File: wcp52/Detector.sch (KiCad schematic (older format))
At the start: 13 parts, among them U10 AD8310ARMZ

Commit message: BOM line fixes
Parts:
- C63, C65, C67, C68, C69, C70, C71, R78, R79, R80: Manuf Value -> (none)
- C64, C66: Description (none) -> CAP MLCC 1uF [0805]
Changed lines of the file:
@@
 EESchema Schematic File Version 2
+LIBS:Altera
+LIBS:AnalogDevices
+LIBS:Atmel
+LIBS:conn-2mm
+LIBS:conn-100mil
+LIBS:conn-cui
+LIBS:conn-fci
+LIBS:conn-linx
+LIBS:conn-molex
+LIBS:conn-tagconnect
+LIBS:conn-test
+LIBS:DiodesInc
+LIBS:display
+LIBS:_electromech
+LIBS:Fairchild
+LIBS:FTDI
+LIBS:Intersil
+LIBS:Lattice
+LIBS:_linear
+LIBS:LinearTech
+LIBS:Littelfuse
+LIBS:logic-4000
+LIBS:logic-7400
+LIBS:MACOM
+LIBS:maxim
+LIBS:mechanical
+LIBS:Microchip
+LIBS:Micron
+LIBS:NXP
+LIBS:onsemi
+LIBS:passive
+LIBS:pasv-BiTech
+LIBS:pasv-Bourns
+LIBS:pasv-cap
+LIBS:pasv-ind
+LIBS:pasv-res
+LIBS:pcb
+LIBS:power
+LIBS:_semi
+LIBS:semi-diode-1N
+LIBS:semi-diode-BA
+LIBS:semi-diode-MCC
+LIBS:semi-diode-MMB
+LIBS:semi-diode-NXP
+LIBS:semi-diode-OnSemi
+LIBS:semi-diode-Vishay
+LIBS:semi-opto-misc
+LIBS:semi-thyristor-2N
+LIBS:semi-trans-2N
+LIBS:semi-trans-AO
+LIBS:semi-trans-BC
+LIBS:semi-trans-DiodesInc
+LIBS:semi-trans-Fairchild
+LIBS:semi-trans-Infineon
+LIBS:semi-trans-IntRect
+LIBS:semi-trans-IXYS
+LIBS:semi-trans-misc
+LIBS:semi-trans-MMB
+LIBS:semi-trans-MPS
+LIBS:semi-trans-NXP
+LIBS:semi-trans-PZT
+LIBS:semi-trans-TI
+LIBS:semi-trans-TIP
+LIBS:semi-trans-Toshiba
+LIBS:silabs
+LIBS:skyworks
+LIBS:ST
+LIBS:st_ic
+LIBS:st_semi
+LIBS:supertex
+LIBS:symbol
+LIBS:TexasInstruments
+LIBS:vishay_semi
+LIBS:Xilinx
+LIBS:pasv-xtal
+LIBS:conn-te
 LIBS:wcp52-cache
 EELAYER 25 0
@@
 F 5 "TDK" H 3700 3600 60  0001 C CNN "Manuf"
 F 6 "DIST DIGIKEY 445-11490-1-ND" H 4500 4150 60  0001 C CNN "BOM"
-F 7 "C78" H 3700 3600 50  0001 C CNN "OldReference"
+F 7 "CAP MLCC 1uF [0805]" H 3700 3600 60  0001 C CNN "Description"
+F 8 "C78" H 3700 3600 50  0001 C CNN "OldReference"
 	1    3700 3600
 	0    1    1    0
@@
 F 5 "TDK" H 3700 4400 60  0001 C CNN "Manuf"
 F 6 "DIST DIGIKEY 445-11490-1-ND" H 4500 4950 60  0001 C CNN "BOM"
-F 7 "C80" H 3700 4400 50  0001 C CNN "OldReference"
+F 7 "CAP MLCC 1uF [0805]" H 3700 4400 60  0001 C CNN "Description"
+F 8 "C80" H 3700 4400 50  0001 C CNN "OldReference"
 	1    3700 4400
 	0    1    1    0
@@
 F 2 "IPC7351-Nominal:CAPC1608X55" H 8200 3800 50  0001 C CNN
 F 3 "" H 8190 3775 60  0000 C CNN
-F 4 "Value" H 8200 3800 60  0001 C CNN "Manuf"
+F 4 "" H 8200 3800 60  0001 C CNN "Manuf"
 F 5 "CAP MLCC 220p C0G 16V 5% [0603]" H 9000 4350 60  0001 C CNN "BOM"
 F 6 "C84" H 8200 3800 50  0001 C CNN "OldReference"
@@
 F 2 "IPC7351-Nominal:CAPC1608X55" H 8200 4600 50  0001 C CNN
 F 3 "" H 8190 4575 60  0000 C CNN
-F 4 "Value" H 8200 4600 60  0001 C CNN "Manuf"
+F 4 "" H 8200 4600 60  0001 C CNN "Manuf"
 F 5 "CAP MLCC 330n ≥X7R 50V 5% [0603]" H 9000 5150 60  0001 C CNN "BOM"
 F 6 "C85" H 8200 4600 50  0001 C CNN "OldReference"
@@
 F 2 "IPC7351-Nominal:CAPC3216X70" H 7100 2700 50  0001 C CNN
 F 3 "" H 7090 2675 60  0000 C CNN
-F 4 "Value" H 7100 2700 60  0001 C CNN "Manuf"
+F 4 "" H 7100 2700 60  0001 C CNN "Manuf"
 F 5 "CAP MLCC 47u ≥X5R 10V 20% [1206]" H 7900 3250 60  0001 C CNN "BOM"
 F 6 "C83" H 7100 2700 50  0001 C CNN "OldReference"
@@
 F 2 "IPC7351-Nominal:CAPC1608X55" H 3700 3400 50  0001 C CNN
 F 3 "" H 3690 3375 60  0000 C CNN
-F 4 "Value" H 3700 3400 60  0001 C CNN "Manuf"
+F 4 "" H 3700 3400 60  0001 C CNN "Manuf"
 F 5 "CAP MLCC 10n ≥X5R 50V 10% [0603]" H 4500 3950 60  0001 C CNN "BOM"
 F 6 "C57" H 3700 3400 50  0001 C CNN "OldReference"
@@
 F 2 "IPC7351-Nominal:CAPC1608X55" H 3700 4200 50  0001 C CNN
 F 3 "" H 3690 4175 60  0000 C CNN
-F 4 "Value" H 3700 4200 60  0001 C CNN "Manuf"
+F 4 "" H 3700 4200 60  0001 C CNN "Manuf"
 F 5 "CAP MLCC 10n ≥X5R 50V 10% [0603]" H 4500 4750 60  0001 C CNN "BOM"
 F 6 "C58" H 3700 4200 50  0001 C CNN "OldReference"
@@
 F 2 "IPC7351-Nominal:CAPC1608X55" H 6000 2700 50  0001 C CNN
 F 3 "" H 5990 2675 60  0000 C CNN
-F 4 "Value" H 6000 2700 60  0001 C CNN "Manuf"
+F 4 "" H 6000 2700 60  0001 C CNN "Manuf"
 F 5 "CAP MLCC 10n ≥X5R 50V 10% [0603]" H 6800 3250 60  0001 C CNN "BOM"
 F 6 "C59" H 6000 2700 50  0001 C CNN "OldReference"
@@
 F 2 "IPC7351-Nominal:CAPC1608X55" H 6500 2700 50  0001 C CNN
 F 3 "" H 6490 2675 60  0000 C CNN
-F 4 "Value" H 6500 2700 60  0001 C CNN "Manuf"
+F 4 "" H 6500 2700 60  0001 C CNN "Manuf"
 F 5 "CAP MLCC 100n ≥X7R 16V 10% [0603]" H 7300 3250 60  0001 C CNN "BOM"
 F 6 "C60" H 6500 2700 50  0001 C CNN "OldReference"
@@
 F 2 "IPC7351-Nominal:RESC1608X50" H 2600 3900 50  0001 C CNN
 F 3 "" H 2600 3950 60  0000 C CNN
-F 4 "Value" H 2600 3900 60  0001 C CNN "Manuf"
+F 4 "" H 2600 3900 60  0001 C CNN "Manuf"
 F 5 "RES SMD 3.3k 5% [0603]" H 3350 4450 60  0001 C CNN "BOM"
 F 6 "R79" H 2600 3900 50  0001 C CNN "OldReference"
@@
 F 2 "IPC7351-Nominal:RESC1608X50" H 3000 3900 50  0001 C CNN
 F 3 "" H 3000 3950 60  0000 C CNN
-F 4 "Value" H 3000 3900 60  0001 C CNN "Manuf"
+F 4 "" H 3000 3900 60  0001 C CNN "Manuf"
 F 5 "RES SMD 53.6 1% [0603]" H 3750 4450 60  0001 C CNN "BOM"
 F 6 "R80" H 3000 3900 50  0001 C CNN "OldReference"
@@
 F 2 "IPC7351-Nominal:RESC1608X50" H 5400 2200 50  0001 C CNN
 F 3 "" H 5400 2250 60  0000 C CNN
-F 4 "Value" H 5400 2200 60  0001 C CNN "Manuf"
+F 4 "" H 5400 2200 60  0001 C CNN "Manuf"
 F 5 "RES SMD 49.9 1% [0603]" H 6150 2750 60  0001 C CNN "BOM"
 F 6 "R81" H 5400 2200 50  0001 C CNN "OldReference"

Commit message: Widen tolerance on a capacitor
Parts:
- C71: BOM CAP MLCC 330n ≥X7R 50V 5% [0603] -> CAP MLCC 330n ≥X7R 50V 10% [0603]
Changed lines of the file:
@@
 F 3 "" H 8190 4575 60  0000 C CNN
 F 4 "" H 8200 4600 60  0001 C CNN "Manuf"
-F 5 "CAP MLCC 330n ≥X7R 50V 5% [0603]" H 9000 5150 60  0001 C CNN "BOM"
+F 5 "CAP MLCC 330n ≥X7R 50V 10% [0603]" H 9000 5150 60  0001 C CNN "BOM"
 F 6 "C85" H 8200 4600 50  0001 C CNN "OldReference"
 	1    8200 4600

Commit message: Schematic/doc work
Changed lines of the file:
@@
 Sheet 10 13
 Title "Logarithmic Detector"
-Date "2015-03-13"
+Date "2015-03-21"
 Rev ""
 Comp "WCP52"
@@
 Comment2 ""
 Comment3 ""
-Comment4 "Eng: Chris Pavlina"
+Comment4 ""
 $EndDescr
 $Comp
@@
 Wire Wire Line
 	7700 4050 8900 4050
-Text HLabel 8900 4050 2    50   Output ~ 0
+Text HLabel 8900 4050 2    60   Output ~ 0
 OUT
 $Comp
@@
 Wire Wire Line
 	5400 2050 5400 2100
-Text Label 7150 2500 0    50   ~ 0
+Text Label 7150 2500 0    60   ~ 0
 4V6_FILTERED
-Text HLabel 2300 3600 0    50   Input ~ 0
+Text HLabel 2300 3600 0    60   Input ~ 0
 IN
 Connection ~ 2600 3600

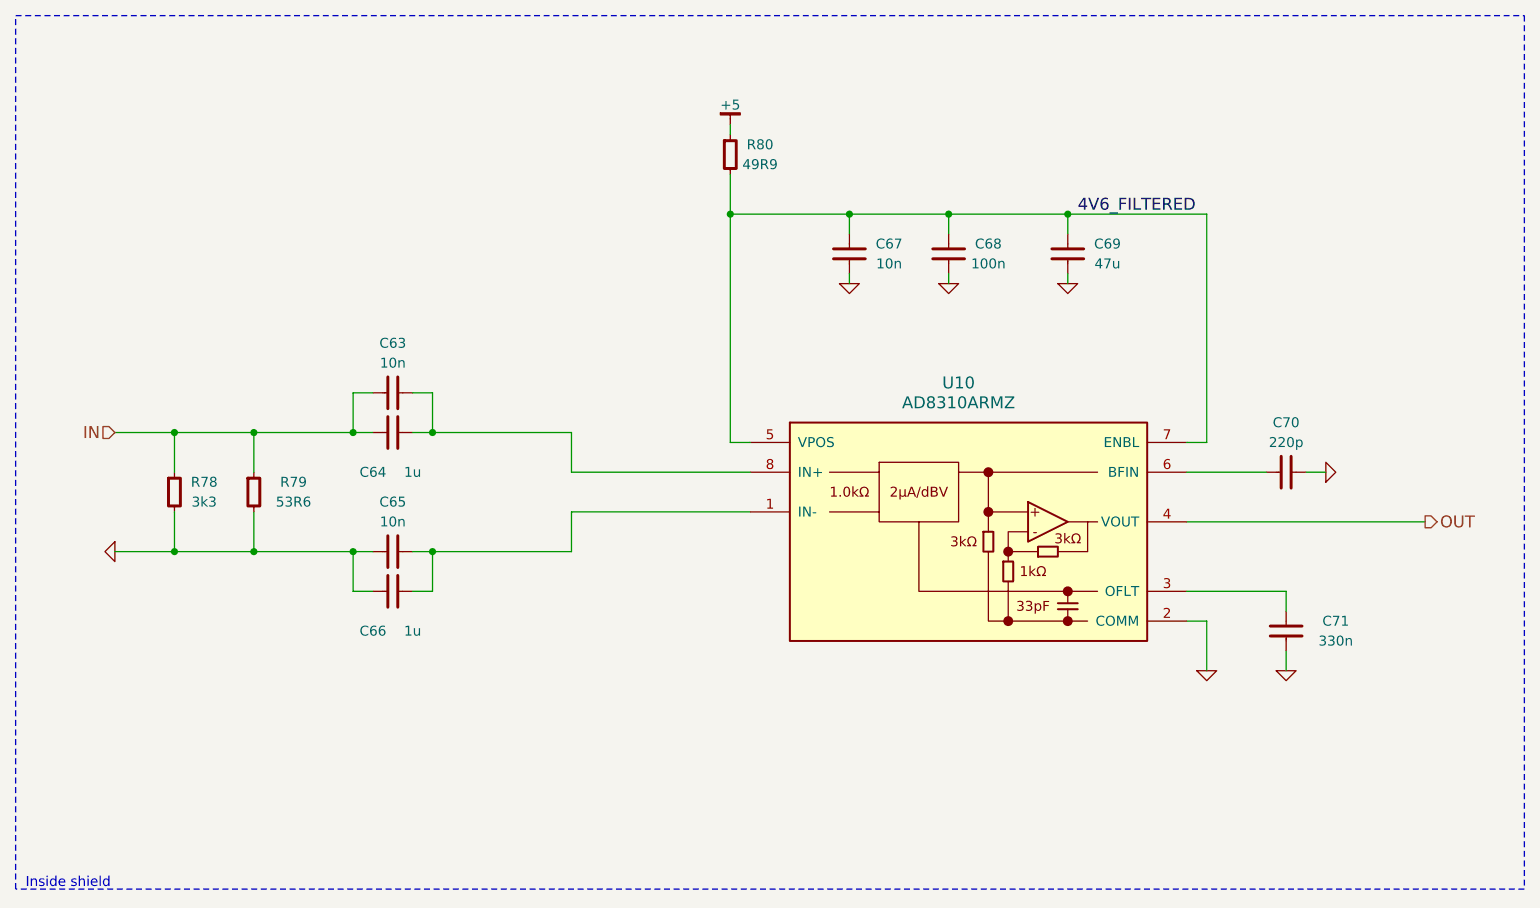
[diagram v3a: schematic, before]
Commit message: Schematic updates for documentation
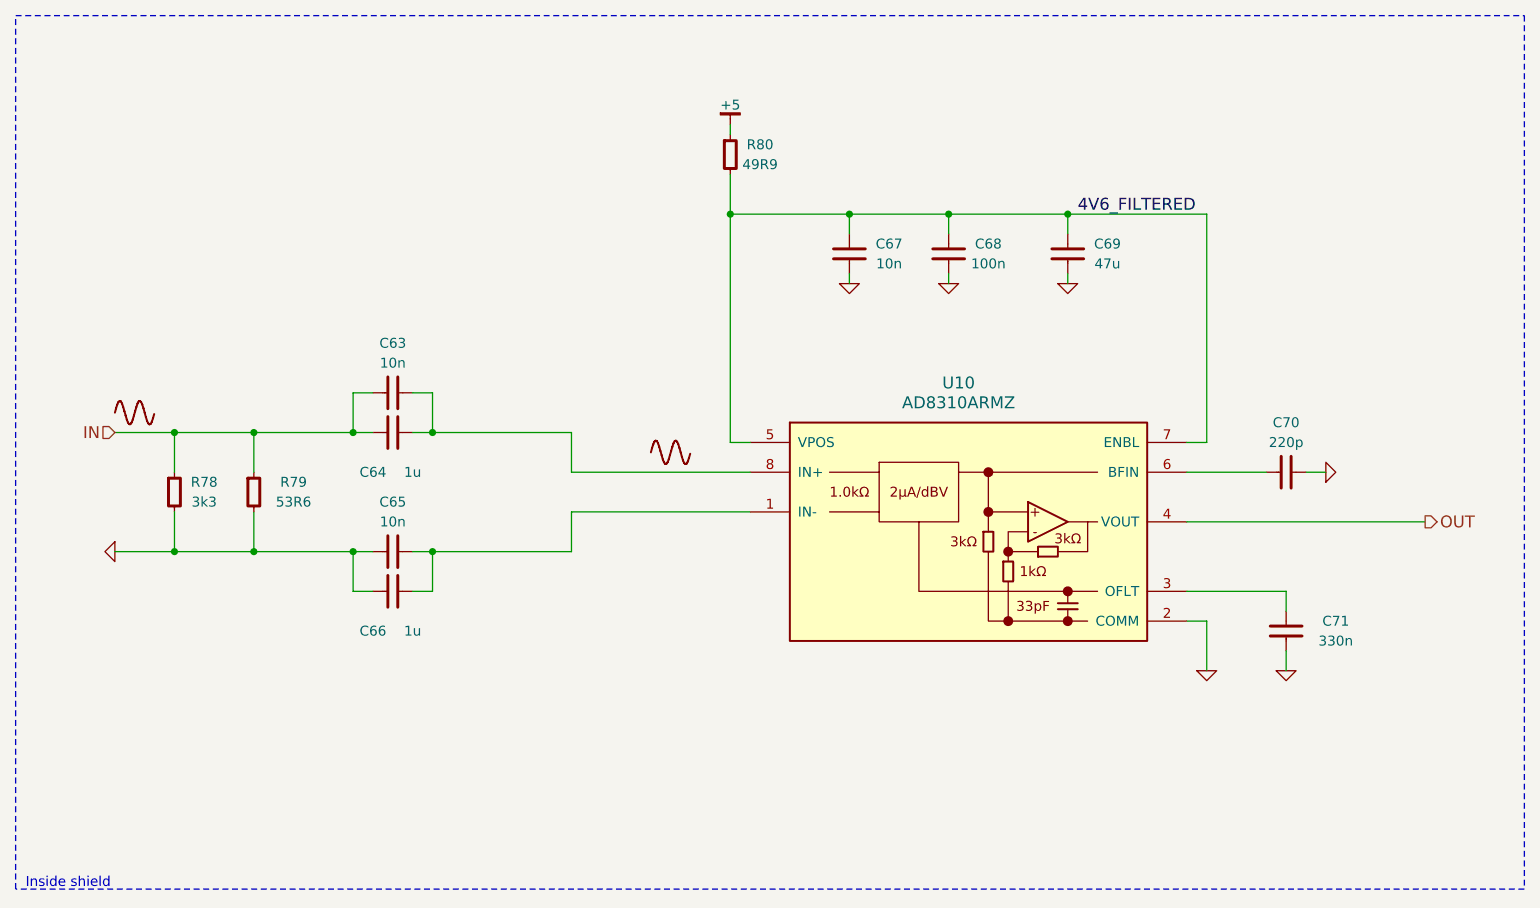
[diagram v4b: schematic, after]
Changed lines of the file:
@@
 	8100 3800 7700 3800
 $Comp
-L GND #PWR0199
+L GND #PWR206
 U 1 1 54F233FD
 P 8400 3800
-F 0 "#PWR0199" H 8400 3800 30  0001 C CNN
+F 0 "#PWR206" H 8400 3800 30  0001 C CNN
 F 1 "GND" H 8400 3730 30  0001 C CNN
 F 2 "" H 8400 3800 60  0000 C CNN
@@
 	8200 4400 7700 4400
 $Comp
-L GND #PWR0200
+L GND #PWR205
 U 1 1 54F23584
 P 8200 4800
-F 0 "#PWR0200" H 8200 4800 30  0001 C CNN
+F 0 "#PWR205" H 8200 4800 30  0001 C CNN
 F 1 "GND" H 8200 4730 30  0001 C CNN
 F 2 "" H 8200 4800 60  0000 C CNN
@@
 	8200 4800 8200 4700
 $Comp
-L GND #PWR0201
+L GND #PWR204
 U 1 1 54F235D2
 P 7800 4800
-F 0 "#PWR0201" H 7800 4800 30  0001 C CNN
+F 0 "#PWR204" H 7800 4800 30  0001 C CNN
 F 1 "GND" H 7800 4730 30  0001 C CNN
 F 2 "" H 7800 4800 60  0000 C CNN
@@
 	7700 3650 7800 3650
 Wire Wire Line
-	7800 2500 7800 3650
-Wire Wire Line
-	5400 2500 7800 2500
+	7800 3650 7800 2500
+Wire Wire Line
+	7800 2500 5400 2500
 $Comp
 L C-1206 C69
@@
 	7100 2500 7100 2600
 $Comp
-L GND #PWR0202
+L GND #PWR203
 U 1 1 54F23A44
 P 7100 2850
-F 0 "#PWR0202" H 7100 2850 30  0001 C CNN
+F 0 "#PWR203" H 7100 2850 30  0001 C CNN
 F 1 "GND" H 7100 2780 30  0001 C CNN
 F 2 "" H 7100 2850 60  0000 C CNN
@@
 	7100 2850 7100 2800
 $Comp
-L GND #PWR0203
+L GND #PWR202
 U 1 1 54F23F3E
 P 6500 2850
-F 0 "#PWR0203" H 6500 2850 30  0001 C CNN
+F 0 "#PWR202" H 6500 2850 30  0001 C CNN
 F 1 "GND" H 6500 2780 30  0001 C CNN
 F 2 "" H 6500 2850 60  0000 C CNN
@@
 Connection ~ 6500 2500
 $Comp
-L GND #PWR0204
+L GND #PWR201
 U 1 1 54F24135
 P 6000 2850
-F 0 "#PWR0204" H 6000 2850 30  0001 C CNN
+F 0 "#PWR201" H 6000 2850 30  0001 C CNN
 F 1 "GND" H 6000 2780 30  0001 C CNN
 F 2 "" H 6000 2850 60  0000 C CNN
@@
 Connection ~ 5400 2500
 $Comp
-L +5 #PWR0205
+L +5 #PWR200
 U 1 1 54F24371
 P 5400 2050
-F 0 "#PWR0205" H 5400 2100 30  0001 C CNN
+F 0 "#PWR200" H 5400 2100 30  0001 C CNN
 F 1 "+5" H 5400 2150 50  0000 C CNN
 F 2 "" H 5400 2050 60  0000 C CNN
@@
 Connection ~ 2600 3600
 $Comp
-L GND #PWR0206
+L GND #PWR199
 U 1 1 54F24ACA
 P 2300 4200
-F 0 "#PWR0206" H 2300 4200 30  0001 C CNN
+F 0 "#PWR199" H 2300 4200 30  0001 C CNN
 F 1 "GND" H 2300 4130 30  0001 C CNN
 F 2 "" H 2300 4200 60  0000 C CNN
@@
 Text Notes 1850 5900 0    50   ~ 0
 Inside shield
+$Comp
+L SINE-ACCURATE #SYM70
+U 1 1 550F58A4
+P 2400 3500
+F 0 "#SYM70" H 2400 3500 60  0001 C CNN
+F 1 "SINE-ACCURATE" H 2400 3500 60  0001 C CNN
+F 2 "" H 2400 3500 60  0000 C CNN
+F 3 "" H 2400 3500 60  0000 C CNN
+	1    2400 3500
+	1    0    0    -1
+$EndComp
+$Comp
+L SINE-ACCURATE #SYM71
+U 1 1 550F592B
+P 5100 3700
+F 0 "#SYM71" H 5100 3700 60  0001 C CNN
+F 1 "SINE-ACCURATE" H 5100 3700 60  0001 C CNN
+F 2 "" H 5100 3700 60  0000 C CNN
+F 3 "" H 5100 3700 60  0000 C CNN
+	1    5100 3700
+	1    0    0    -1
+$EndComp
 $EndSCHEMATC

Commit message: More doc fixes
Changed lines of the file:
@@
 Inside shield
 $Comp
-L SINE-ACCURATE #SYM70
+L SINE-ACCURATE #SYM80
 U 1 1 550F58A4
 P 2400 3500
-F 0 "#SYM70" H 2400 3500 60  0001 C CNN
+F 0 "#SYM80" H 2400 3500 60  0001 C CNN
 F 1 "SINE-ACCURATE" H 2400 3500 60  0001 C CNN
 F 2 "" H 2400 3500 60  0000 C CNN
@@
 $EndComp
 $Comp
-L SINE-ACCURATE #SYM71
+L SINE-ACCURATE #SYM81
 U 1 1 550F592B
 P 5100 3700
-F 0 "#SYM71" H 5100 3700 60  0001 C CNN
+F 0 "#SYM81" H 5100 3700 60  0001 C CNN
 F 1 "SINE-ACCURATE" H 5100 3700 60  0001 C CNN
 F 2 "" H 5100 3700 60  0000 C CNN
@@
 	1    0    0    -1
 $EndComp
+Wire Wire Line
+	2300 3600 2325 3625
+Wire Wire Line
+	2325 3625 3575 3625
+Wire Wire Line
+	3575 3625 3600 3600
+Wire Wire Line
+	3800 3600 3825 3625
+Wire Wire Line
+	3825 3625 4575 3625
+Wire Wire Line
+	4575 3625 4575 3825
+Wire Wire Line
+	4575 3825 5475 3825
+Wire Wire Line
+	5475 3825 5500 3800
+Wire Wire Line
+	7700 4050 7725 4075
+Wire Wire Line
+	7725 4075 8875 4075
+Wire Wire Line
+	8875 4075 8900 4050
 $EndSCHEMATC

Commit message: Nicer BOM lines
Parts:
- C63: OldReference C57 -> (none)
- C64: OldReference C78 -> (none)
- C65: OldReference C58 -> (none)
- C66: OldReference C80 -> (none)
- C67: OldReference C59 -> (none)
- C68: OldReference C60 -> (none)
- C69: OldReference C83 -> (none)
- C70: OldReference C84 -> (none)
- C71: OldReference C85 -> (none)
- R78: OldReference R79 -> (none)
- R79: OldReference R80 -> (none)
- R80: OldReference R81 -> (none)
- U10: OldReference U11 -> (none)
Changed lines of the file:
@@
 F 6 "DIST DIGIKEY 445-11490-1-ND" H 4500 4150 60  0001 C CNN "BOM"
 F 7 "CAP MLCC 1uF [0805]" H 3700 3600 60  0001 C CNN "Description"
-F 8 "C78" H 3700 3600 50  0001 C CNN "OldReference"
 	1    3700 3600
 	0    1    1    0
@@
 F 6 "DIST DIGIKEY 445-11490-1-ND" H 4500 4950 60  0001 C CNN "BOM"
 F 7 "CAP MLCC 1uF [0805]" H 3700 4400 60  0001 C CNN "Description"
-F 8 "C80" H 3700 4400 50  0001 C CNN "OldReference"
 	1    3700 4400
 	0    1    1    0
@@
 F 5 "AnalogDevices" H 6550 4050 60  0001 C CNN "Manuf"
 F 6 "IC ADI AD8310ARMZ" H 7050 5250 60  0001 C CNN "BOM"
-F 7 "U11" H 6550 4050 50  0001 C CNN "OldReference"
 	1    6550 4050
 	1    0    0    -1
@@
 F 4 "" H 8200 3800 60  0001 C CNN "Manuf"
 F 5 "CAP MLCC 220p C0G 16V 5% [0603]" H 9000 4350 60  0001 C CNN "BOM"
-F 6 "C84" H 8200 3800 50  0001 C CNN "OldReference"
 	1    8200 3800
 	0    1    1    0
@@
 F 2 "" H 8400 3800 60  0000 C CNN
 F 3 "" H 8400 3800 60  0000 C CNN
-F 4 "#PWR0198" H 8400 3800 50  0001 C CNN "OldReference"
 	1    8400 3800
 	0    -1   -1   0
@@
 F 4 "" H 8200 4600 60  0001 C CNN "Manuf"
 F 5 "CAP MLCC 330n ≥X7R 50V 10% [0603]" H 9000 5150 60  0001 C CNN "BOM"
-F 6 "C85" H 8200 4600 50  0001 C CNN "OldReference"
 	1    8200 4600
 	1    0    0    -1
@@
 F 2 "" H 8200 4800 60  0000 C CNN
 F 3 "" H 8200 4800 60  0000 C CNN
-F 4 "#PWR0199" H 8200 4800 50  0001 C CNN "OldReference"
 	1    8200 4800
 	1    0    0    -1
@@
 F 2 "" H 7800 4800 60  0000 C CNN
 F 3 "" H 7800 4800 60  0000 C CNN
-F 4 "#PWR0200" H 7800 4800 50  0001 C CNN "OldReference"
 	1    7800 4800
 	1    0    0    -1
@@
 F 4 "" H 7100 2700 60  0001 C CNN "Manuf"
 F 5 "CAP MLCC 47u ≥X5R 10V 20% [1206]" H 7900 3250 60  0001 C CNN "BOM"
-F 6 "C83" H 7100 2700 50  0001 C CNN "OldReference"
 	1    7100 2700
 	1    0    0    -1
@@
 F 2 "" H 7100 2850 60  0000 C CNN
 F 3 "" H 7100 2850 60  0000 C CNN
-F 4 "#PWR0201" H 7100 2850 50  0001 C CNN "OldReference"
 	1    7100 2850
 	1    0    0    -1
@@
 F 2 "" H 6500 2850 60  0000 C CNN
 F 3 "" H 6500 2850 60  0000 C CNN
-F 4 "#PWR0202" H 6500 2850 50  0001 C CNN "OldReference"
 	1    6500 2850
 	1    0    0    -1
@@
 F 2 "" H 6000 2850 60  0000 C CNN
 F 3 "" H 6000 2850 60  0000 C CNN
-F 4 "#PWR0203" H 6000 2850 50  0001 C CNN "OldReference"
 	1    6000 2850
 	1    0    0    -1
@@
 F 2 "" H 5400 2050 60  0000 C CNN
 F 3 "" H 5400 2050 60  0000 C CNN
-F 4 "#PWR0204" H 5400 2050 50  0001 C CNN "OldReference"
 	1    5400 2050
 	1    0    0    -1
@@
 F 2 "" H 2300 4200 60  0000 C CNN
 F 3 "" H 2300 4200 60  0000 C CNN
-F 4 "#PWR0205" H 2300 4200 50  0001 C CNN "OldReference"
 	1    2300 4200
 	0    1    1    0
@@
 F 4 "" H 3700 3400 60  0001 C CNN "Manuf"
 F 5 "CAP MLCC 10n ≥X5R 50V 10% [0603]" H 4500 3950 60  0001 C CNN "BOM"
-F 6 "C57" H 3700 3400 50  0001 C CNN "OldReference"
 	1    3700 3400
 	0    1    -1   0
@@
 F 4 "" H 3700 4200 60  0001 C CNN "Manuf"
 F 5 "CAP MLCC 10n ≥X5R 50V 10% [0603]" H 4500 4750 60  0001 C CNN "BOM"
-F 6 "C58" H 3700 4200 50  0001 C CNN "OldReference"
 	1    3700 4200
 	0    1    -1   0
@@
 F 4 "" H 6000 2700 60  0001 C CNN "Manuf"
 F 5 "CAP MLCC 10n ≥X5R 50V 10% [0603]" H 6800 3250 60  0001 C CNN "BOM"
-F 6 "C59" H 6000 2700 50  0001 C CNN "OldReference"
 	1    6000 2700
 	1    0    0    -1
@@
 F 4 "" H 6500 2700 60  0001 C CNN "Manuf"
 F 5 "CAP MLCC 100n ≥X7R 16V 10% [0603]" H 7300 3250 60  0001 C CNN "BOM"
-F 6 "C60" H 6500 2700 50  0001 C CNN "OldReference"
 	1    6500 2700
 	1    0    0    -1
@@
 F 4 "" H 2600 3900 60  0001 C CNN "Manuf"
 F 5 "RES SMD 3.3k 5% [0603]" H 3350 4450 60  0001 C CNN "BOM"
-F 6 "R79" H 2600 3900 50  0001 C CNN "OldReference"
 	1    2600 3900
 	1    0    0    -1
@@
 F 4 "" H 3000 3900 60  0001 C CNN "Manuf"
 F 5 "RES SMD 53.6 1% [0603]" H 3750 4450 60  0001 C CNN "BOM"
-F 6 "R80" H 3000 3900 50  0001 C CNN "OldReference"
 	1    3000 3900
 	1    0    0    -1
@@
 F 4 "" H 5400 2200 60  0001 C CNN "Manuf"
 F 5 "RES SMD 49.9 1% [0603]" H 6150 2750 60  0001 C CNN "BOM"
-F 6 "R81" H 5400 2200 50  0001 C CNN "OldReference"
 	1    5400 2200
 	1    0    0    -1
